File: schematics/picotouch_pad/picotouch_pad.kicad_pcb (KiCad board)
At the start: 2 copper layers, 193.5 x 38 mm, 101 parts, among them J1 AudioJack4, SW1 SSSS811101, U1 Pico, U2 MCP73831-2-OT, X1 AFC20-S02ACA-00

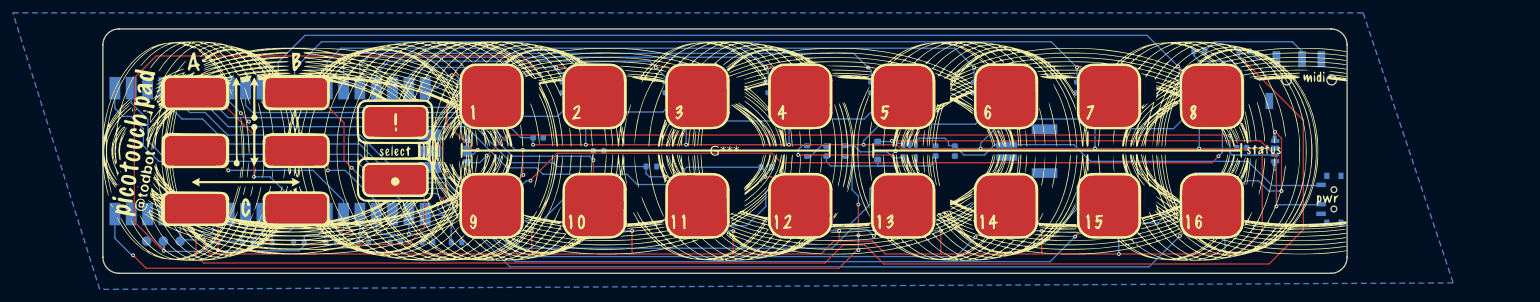
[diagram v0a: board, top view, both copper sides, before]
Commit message: resize, cleanup, change battery charge chip sch symbol
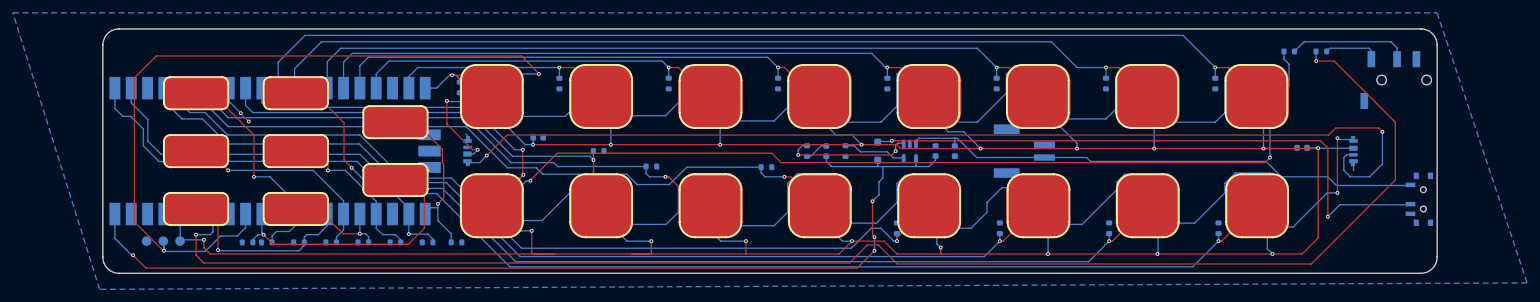
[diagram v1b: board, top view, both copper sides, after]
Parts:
- removed G***: LOGO, LOGO
- moved J1 14.8 mm to (215.2, 34.3)
- moved R27 14.0 mm to (198.6, 29.9)
- moved SW1 13.9 mm to (219.0, 52.9)
- moved LED17 12.2 mm to (208.6, 45.4)
- moved R26 12.0 mm to (203.6, 29.9)
- moved C17 9.40 mm to (200.6, 44.9)
- moved LED16 7.40 mm to (197.6, 52.9)
- moved LED8 7.40 mm to (197.6, 36.0)
- moved C8 7.03 mm to (193.6, 34.9)
- moved C16 7.00 mm to (193.6, 53.4)
- moved PAD16 7.00 mm to (193.6, 53.9)
- moved PAD8 7.00 mm to (193.6, 36.9)
- moved LED15 6.40 mm to (180.6, 52.9)
- moved LED7 6.40 mm to (180.6, 36.0)
- moved C7 6.03 mm to (176.6, 34.9)
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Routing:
- net Net-(LED17-DOUT): track 130.3 -> 160.7 mm
- net +3.3V: track 592.3 -> 612.9 mm
- net Net-(D2-A): track 77.9 -> 94.5 mm
- net +BATT: track 68.4 -> 81.4 mm
- net /MIDI_OUT: track 218.8 -> 231.2 mm
- net Net-(LED8-DOUT): track 123.8 -> 132.0 mm
- net Net-(LED16-DOUT): track 21.7 -> 27.9 mm
- net /TOUCH8: track 158.4 -> 164.5 mm
- net /TOUCH7: track 138.2 -> 143.5 mm
- net /TOUCH5: track 97.8 -> 102.2 mm
- net Net-(J1-PadT): track 4.67 -> 8.64 mm
- net /TOUCH16: track 193.1 -> 196.7 mm
- net Net-(LED11-DOUT): track 27.1 -> 30.7 mm
- net /TOUCH6: track 116.9 -> 120.0 mm
- net /TOUCH13: track 130.0 -> 133.1 mm
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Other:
- board size 193.5 x 38 mm -> 207.5 x 38 mm
- board text added: "- +"
- board text added: "picotouch_pad - USB MIDI controller / macropad 22 Sep 2024 - @todbot / Tod Kurt github.com/todbot/picotouch_pad Uses Pico RP2040"
- board text removed: "${REFERENCE}"
- board text removed: "picotouch_pad - USB MIDI controller / macropad 15 Sep 2024 - @todbot / Tod Kurt github.com/todbot/picotouch_pad Uses Pico RP2040"
